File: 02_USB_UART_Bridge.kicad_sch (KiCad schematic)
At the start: 1 part, among them U1 CP2102N-Axx-xQFN24

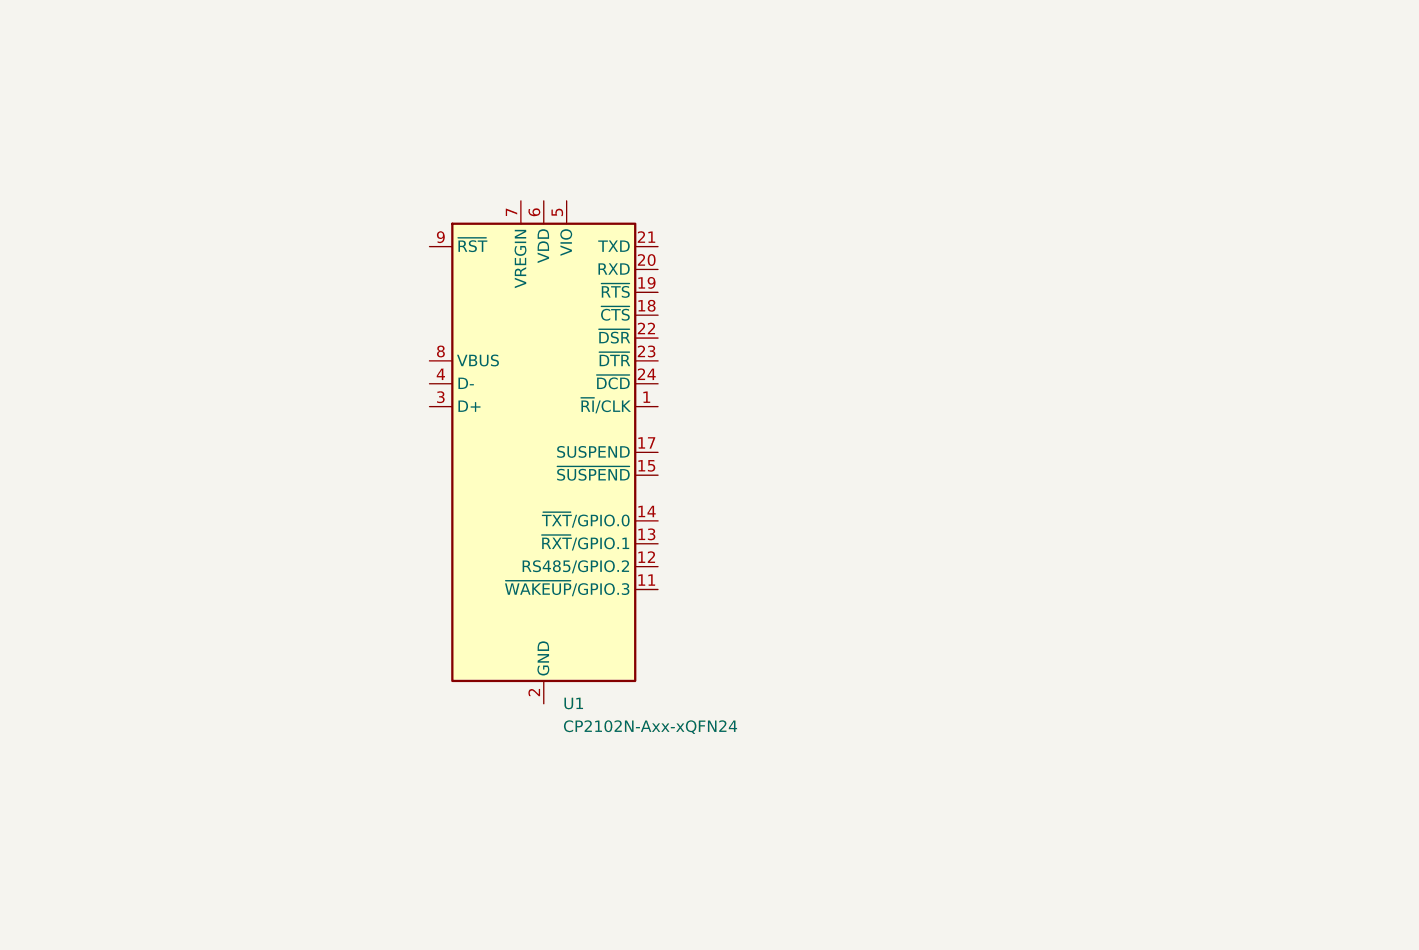
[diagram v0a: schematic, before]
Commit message: completed schematic design, and selected all footprints and for now will go for 0805 for resistors, capacitors and leds - will later make a call during layoting
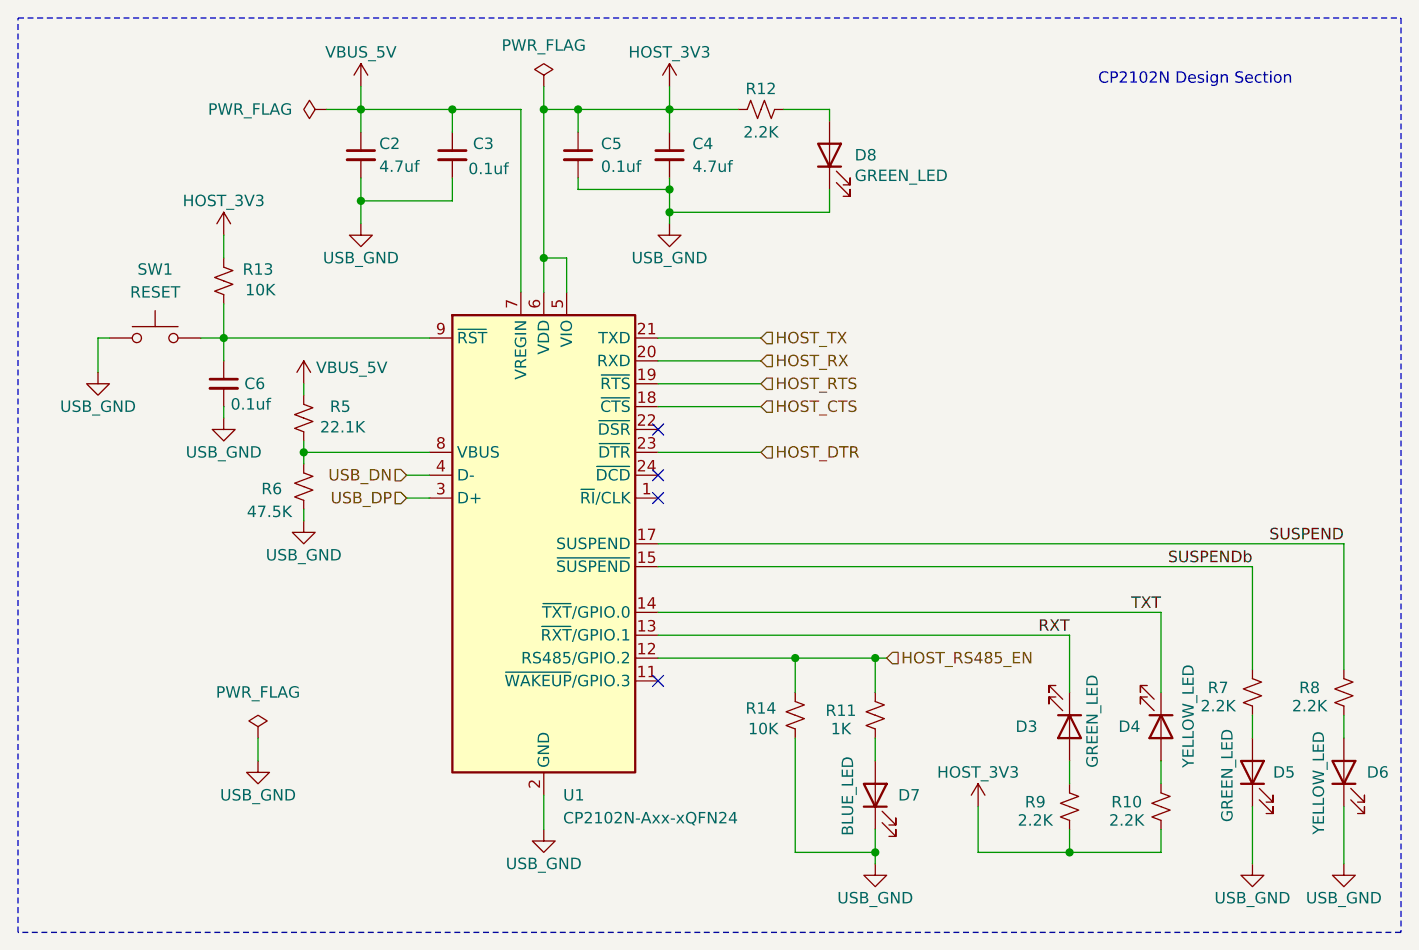
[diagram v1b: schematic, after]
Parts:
- added C2, C4: 4.7uf, Capacitor_SMD:C_0805_2012Metric_Pad1.18x1.45mm_HandSolder, symbol Device:C_Small
- added C3, C5, C6: 0.1uf, Capacitor_SMD:C_0805_2012Metric_Pad1.18x1.45mm_HandSolder, symbol Device:C_Small
- added D3, D5, D8: GREEN_LED, LED_SMD:LED_0805_2012Metric_Pad1.15x1.40mm_HandSolder, symbol Device:LED
- added D4, D6: YELLOW_LED, LED_SMD:LED_0805_2012Metric_Pad1.15x1.40mm_HandSolder, symbol Device:LED
- added D7: BLUE_LED, LED_SMD:LED_0805_2012Metric_Pad1.15x1.40mm_HandSolder, symbol Device:LED
- added R10, R12, R7, R8, R9: 2.2K, Resistor_SMD:R_0805_2012Metric_Pad1.20x1.40mm_HandSolder, symbol Device:R_Small_US
- added R11: 1K, Resistor_SMD:R_0805_2012Metric_Pad1.20x1.40mm_HandSolder, symbol Device:R_Small_US
- added R13, R14: 10K, Resistor_SMD:R_0805_2012Metric_Pad1.20x1.40mm_HandSolder, symbol Device:R_Small_US
- added R5: 22.1K, Resistor_SMD:R_0805_2012Metric_Pad1.20x1.40mm_HandSolder, symbol Device:R_Small_US
- added R6: 47.5K, Resistor_SMD:R_0805_2012Metric_Pad1.20x1.40mm_HandSolder, symbol Device:R_Small_US
- added SW1: RESET, Button_Switch_SMD:SW_SPST_CK_RS282G05A3, symbol Switch:SW_Push
- U1: footprint Package_DFN_QFN:QFN-24-1EP_4x4mm_P0.5mm_EP2.6x2.6mm -> Package_DFN_QFN:QFN-24-1EP_4x4mm_P0.5mm_EP2.6x2.6mm_ThermalVias
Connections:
- net HOST_RS485_EN: now reaches U1.12 (RS485/GPIO.2)
- net HOST_RS485_EN: now also R11.1, R14.2
- net RXT: now reaches U1.13 (~{RXT}/GPIO.1)
- net RXT: now also D3.1 (K)
- net TXT: now reaches U1.14 (~{TXT}/GPIO.0)
- net TXT: now also D4.1 (K)
- net SUSPENDb: now reaches U1.15 (~{SUSPEND})
- net SUSPENDb: now also R7.1
- net SUSPEND: now reaches U1.17 (SUSPEND)
- net SUSPEND: now also R8.1
- net HOST_CTS: now reaches U1.18 (~{CTS})
- net HOST_RTS: now reaches U1.19 (~{RTS})
- net USB_GND: now reaches U1.2 (GND), U1.25 (GND)
- net USB_GND: now also C2.2, C3.2, C4.2, C5.2, C6.2, D5.1 (K), D6.1 (K), D7.1 (K), D8.1 (K), R14.1, R6.2, SW1.1
- net HOST_RX: now reaches U1.20 (RXD)
- net HOST_TX: now reaches U1.21 (TXD)
- net HOST_DTR: now reaches U1.23 (~{DTR})
- net USB_DP: now reaches U1.3 (D+)
- net USB_DN: now reaches U1.4 (D-)
- net HOST_3V3: now reaches U1.5 (VIO)
- net HOST_3V3: now also U1.6 (VDD), C4.1, C5.1, R10.2, R12.1, R13.1, R9.2
- net VBUS_5V: now reaches U1.7 (VREGIN)
- net VBUS_5V: now also C2.1, C3.1, R5.1
- net at U1.8 (VBUS): now also R5.2, R6.1
- net at U1.9 (~{RST}): now also C6.1, R13.2, SW1.2
- new net: D5.2 (A), R7.2
- new net: D7.2 (A), R11.2
- new net: D6.2 (A), R8.2
- new net: D8.2 (A), R12.2
- new net: D4.2 (A), R10.1
- new net: D3.2 (A), R9.1
- no-connect marks 0 -> 4
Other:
- note added: "CP2102N Design Section"
- moved on the sheet: U1
